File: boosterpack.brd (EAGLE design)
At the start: 100 x 80 mm, 17 parts

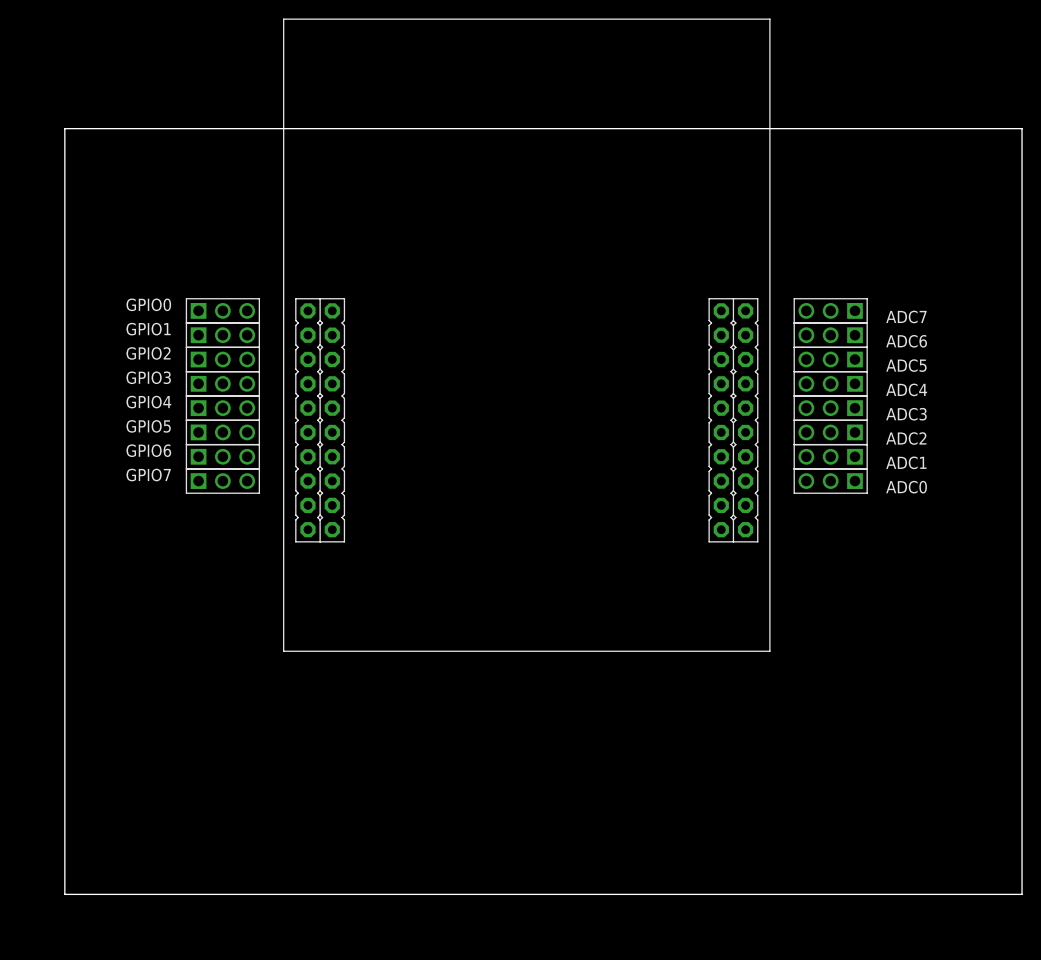
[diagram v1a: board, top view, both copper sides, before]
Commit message: added power regulating circiut
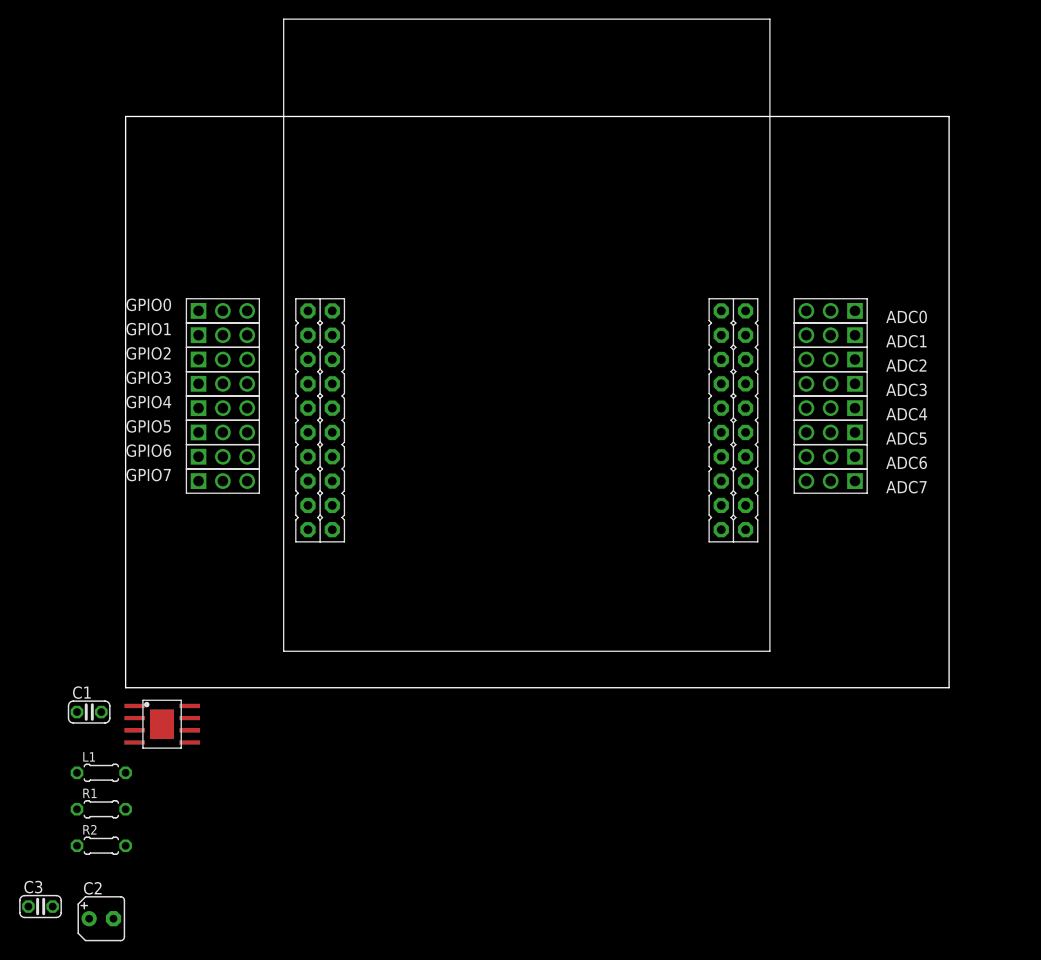
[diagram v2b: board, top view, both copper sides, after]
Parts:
- added C1: 10nF, resistor:C025-024X044
- added C2: 330uF, resistor:B45181A
- added C3: (no value), resistor:C025-024X044
- added L1: 10uH, resistor:0204/5
- added R1: 10k, resistor:0204/5
- added R2: 3.24k, resistor:0204/5
- added U$2: TPS5450, packages(ti):DDS
- moved ADC0 17.8 mm to (82.5, 61.0)
- moved ADC7 17.8 mm to (82.5, 43.2)
- moved ADC1 12.7 mm to (82.5, 58.4)
- moved ADC6 12.7 mm to (82.5, 45.7)
- moved ADC2 7.62 mm to (82.5, 55.9)
- moved ADC5 7.62 mm to (82.5, 48.3)
- moved ADC3 2.54 mm to (82.5, 53.3)
- moved ADC4 2.54 mm to (82.5, 50.8)
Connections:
- removed net GND2: U$1.GND2
- removed net VBUS: U$1.VBUS
- new net +5V: C2.+, L1.2, R1.2, U$1.VBUS
- new net GND: C2.-, C3.2, R2.1, U$1.GND1, U$1.GND2, U$2.6, U$2.GROUNDPAD
- new net N$10: R1.1, R2.2, U$2.4
- new net N$11: C1.1, L1.1, U$2.8
- new net N$9: C1.2, U$2.1
- new net VCC: C3.1, U$2.7
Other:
- board size 100 x 80 mm -> 86 x 59.7 mm
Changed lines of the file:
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@@
 <board>
 <plain>
-<wire x1="0" y1="0" x2="100" y2="0" width="0" layer="20"/>
-<wire x1="100" y1="0" x2="100" y2="80" width="0" layer="20"/>
-<wire x1="100" y1="80" x2="0" y2="80" width="0" layer="20"/>
-<wire x1="0" y1="80" x2="0" y2="0" width="0" layer="20"/>
+<wire x1="6.35" y1="21.59" x2="92.38" y2="21.59" width="0" layer="20"/>
+<wire x1="92.38" y1="21.59" x2="92.38" y2="81.27" width="0" layer="20"/>
+<wire x1="92.38" y1="81.27" x2="6.35" y2="81.27" width="0" layer="20"/>
+<wire x1="6.35" y1="81.27" x2="6.35" y2="21.59" width="0" layer="20"/>
 </plain>
 <attributes>
@@
 <element name="GPIO7" library="RASEagleLib" package="3PINHEADER" value="3PINHEADER" x="13.97" y="43.18"/>
 <element name="GPIO5" library="RASEagleLib" package="3PINHEADER" value="3PINHEADER" x="13.97" y="48.26"/>
-<element name="ADC0" library="RASEagleLib" package="3PINHEADER" value="3PINHEADER" x="82.55" y="43.18" rot="R180"/>
-<element name="ADC2" library="RASEagleLib" package="3PINHEADER" value="3PINHEADER" x="82.55" y="48.26" rot="R180"/>
-<element name="ADC1" library="RASEagleLib" package="3PINHEADER" value="3PINHEADER" x="82.55" y="45.72" rot="R180"/>
-<element name="ADC3" library="RASEagleLib" package="3PINHEADER" value="3PINHEADER" x="82.55" y="50.8" rot="R180"/>
-<element name="ADC7" library="RASEagleLib" package="3PINHEADER" value="3PINHEADER" x="82.55" y="60.96" rot="R180"/>
-<element name="ADC6" library="RASEagleLib" package="3PINHEADER" value="3PINHEADER" x="82.55" y="58.42" rot="R180"/>
-<element name="ADC5" library="RASEagleLib" package="3PINHEADER" value="3PINHEADER" x="82.55" y="55.88" rot="R180"/>
-<element name="ADC4" library="RASEagleLib" package="3PINHEADER" value="3PINHEADER" x="82.55" y="53.34" rot="R180"/>
+<element name="ADC0" library="RASEagleLib" package="3PINHEADER" value="3PINHEADER" x="82.55" y="60.96" rot="R180"/>
+<element name="ADC2" library="RASEagleLib" package="3PINHEADER" value="3PINHEADER" x="82.55" y="55.88" rot="R180"/>
+<element name="ADC1" library="RASEagleLib" package="3PINHEADER" value="3PINHEADER" x="82.55" y="58.42" rot="R180"/>
+<element name="ADC3" library="RASEagleLib" package="3PINHEADER" value="3PINHEADER" x="82.55" y="53.34" rot="R180"/>
+<element name="ADC7" library="RASEagleLib" package="3PINHEADER" value="3PINHEADER" x="82.55" y="43.18" rot="R180"/>
+<element name="ADC6" library="RASEagleLib" package="3PINHEADER" value="3PINHEADER" x="82.55" y="45.72" rot="R180"/>
+<element name="ADC5" library="RASEagleLib" package="3PINHEADER" value="3PINHEADER" x="82.55" y="48.26" rot="R180"/>
+<element name="ADC4" library="RASEagleLib" package="3PINHEADER" value="3PINHEADER" x="82.55" y="50.8" rot="R180"/>
+<element name="U$2" library="packages(ti)" package="DDS" value="TPS5450" x="10.16" y="17.78"/>
+<element name="C1" library="resistor" package="C025-024X044" value="10nF" x="2.54" y="19.05"/>
+<element name="L1" library="resistor" package="0204/5" value="10uH" x="3.81" y="12.7"/>
+<element name="R1" library="resistor" package="0204/5" value="10k" x="3.81" y="8.89"/>
+<element name="R2" library="resistor" package="0204/5" value="3.24k" x="3.81" y="5.08"/>
+<element name="C2" library="resistor" package="B45181A" value="330uF" x="3.81" y="-2.54"/>
+<element name="C3" library="resistor" package="C025-024X044" value="" x="-2.54" y="-1.27"/>
 </elements>
 <signals>
@@
 <contactref element="U$1" pad="3.3V"/>
 </signal>
-<signal name="VBUS">
-<contactref element="U$1" pad="VBUS"/>
-</signal>
 <signal name="RST">
 <contactref element="U$1" pad="RST"/>
-</signal>
-<signal name="GND2">
-<contactref element="U$1" pad="GND2"/>
 </signal>
 <signal name="N$7">
@@
 <contactref element="U$1" pad="PB7"/>
 </signal>
+<signal name="N$9">
+<contactref element="U$2" pad="1"/>
+<contactref element="C1" pad="2"/>
+<wire x1="3.81" y1="19.05" x2="7.285" y2="19.685" width="0" layer="19" extent="1-1"/>
+</signal>
+<signal name="+5V">
+<contactref element="C2" pad="+"/>
+<contactref element="L1" pad="2"/>
+<contactref element="R1" pad="2"/>
+<contactref element="U$1" pad="VBUS"/>
+<wire x1="6.35" y1="12.7" x2="27.94" y2="60.96" width="0" layer="19" extent="1-1"/>
+<wire x1="6.35" y1="8.89" x2="6.35" y2="12.7" width="0" layer="19" extent="1-1"/>
+<wire x1="2.54" y1="-2.54" x2="6.35" y2="8.89" width="0" layer="19" extent="1-1"/>
+</signal>
+<signal name="GND">
+<contactref element="C2" pad="-"/>
+<contactref element="R2" pad="1"/>
+<contactref element="C3" pad="2"/>
+<contactref element="U$2" pad="6"/>
+<contactref element="U$2" pad="GROUNDPAD"/>
+<contactref element="U$1" pad="GND1"/>
+<contactref element="U$1" pad="GND2"/>
+<wire x1="27.94" y1="58.42" x2="71.12" y2="60.96" width="0" layer="19" extent="1-1"/>
+<wire x1="13.035" y1="17.145" x2="27.94" y2="58.42" width="0" layer="19" extent="1-1"/>
+<wire x1="10.16" y1="17.78" x2="13.035" y2="17.145" width="0" layer="19" extent="1-1"/>
+<wire x1="1.27" y1="5.08" x2="10.16" y2="17.78" width="0" layer="19" extent="1-1"/>
+<wire x1="-1.27" y1="-1.27" x2="1.27" y2="5.08" width="0" layer="19" extent="1-1"/>
+<wire x1="5.08" y1="-2.54" x2="-1.27" y2="-1.27" width="0" layer="19" extent="1-1"/>
+</signal>
+<signal name="N$10">
+<contactref element="U$2" pad="4"/>
+<contactref element="R1" pad="1"/>
+<contactref element="R2" pad="2"/>
+<wire x1="1.27" y1="8.89" x2="7.285" y2="15.875" width="0" layer="19" extent="1-1"/>
+<wire x1="6.35" y1="5.08" x2="1.27" y2="8.89" width="0" layer="19" extent="1-1"/>
+</signal>
+<signal name="N$11">
+<contactref element="U$2" pad="8"/>
+<contactref element="L1" pad="1"/>
+<contactref element="C1" pad="1"/>
+<wire x1="1.27" y1="19.05" x2="13.035" y2="19.685" width="0" layer="19" extent="1-1"/>
+<wire x1="1.27" y1="12.7" x2="1.27" y2="19.05" width="0" layer="19" extent="1-1"/>
+</signal>
+<signal name="VCC">
+<contactref element="U$2" pad="7"/>
+<contactref element="C3" pad="1"/>
+<wire x1="-3.81" y1="-1.27" x2="13.035" y2="18.415" width="0" layer="19" extent="1-1"/>
+</signal>
 </signals>

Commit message: new layout for the reg circuit
I feel like explaining my use of the smd inductor
 * it's small ~10mm wide by ~6mm tall
 * it's easy to solder (it's a huge smd part afterall)
 * it's cheip $0.60
 * it makes putting the regulator under the launchpad possible
 * it brings down the surface area by about half compared to other parts
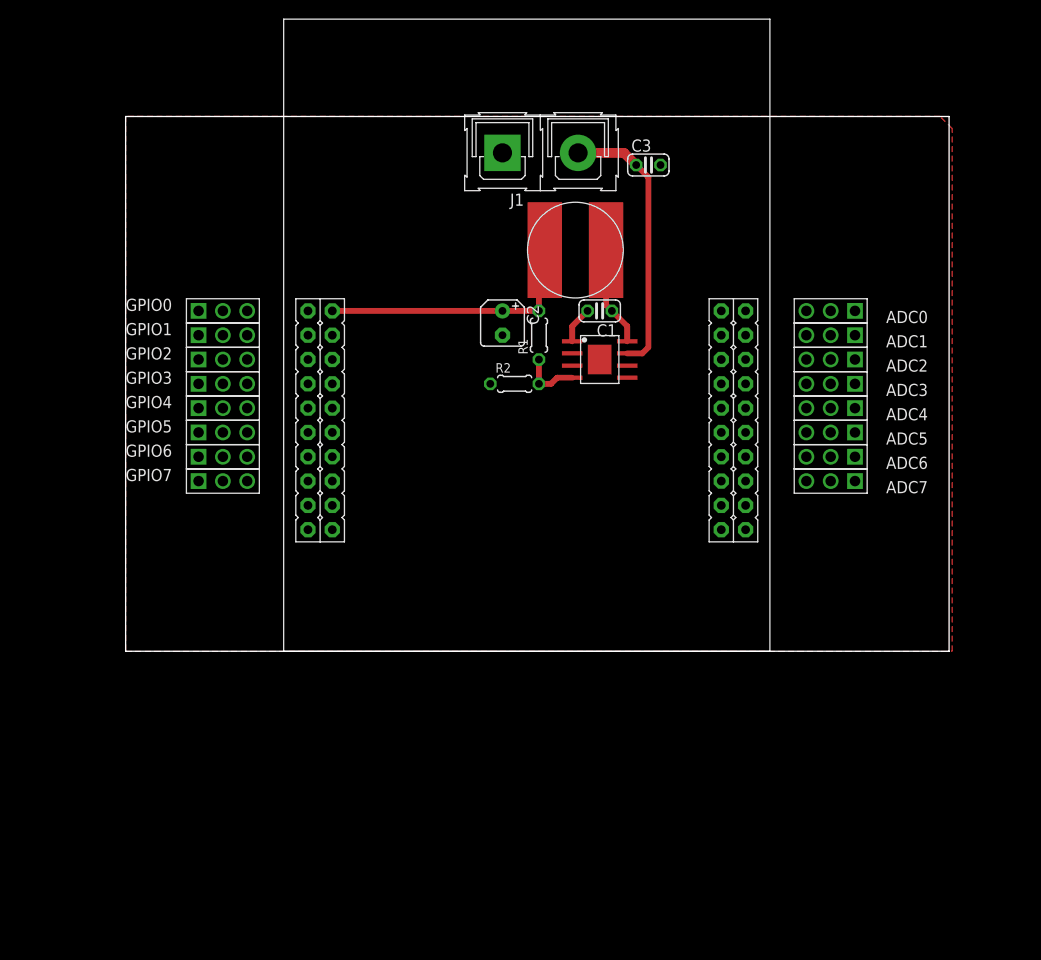
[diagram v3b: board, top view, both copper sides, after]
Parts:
- added J1: POWERPOLE_DOUBLE, RASEagleLib:POWERPOLE_DOUBLE
- L1: device resistor:0204/5 -> RASEagleLib:SDR1006
- moved C3 100.2 mm to (61.0, 76.2)
- moved C2 75.0 mm to (45.7, 59.7), turned to 270 degrees
- moved L1 73.7 mm to (53.3, 67.3), turned to 270 degrees
- moved C1 67.8 mm to (55.9, 61.0), turned to 180 degrees
- moved R1 67.4 mm to (49.5, 58.4), turned to 90 degrees
- moved R2 64.8 mm to (47.0, 53.3)
- moved U$2 59.5 mm to (55.9, 55.9)
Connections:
- net +5V: now also L1.P$2; no longer L1.2
- net GND: now also J1.1
- net N$11: now also L1.P$1; no longer L1.1
- net VCC: now also J1.2
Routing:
- net VCC: track 0.00 -> 28.6 mm
- net +5V: track 0.00 -> 28.2 mm
- net N$11: track 0.00 -> 10.4 mm
- net N$10: track 0.00 -> 6.28 mm
- net N$9: track 0.00 -> 3.84 mm
- added copper zone on layer 1, net GND
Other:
- board size 86 x 59.7 mm -> 86 x 55.9 mm
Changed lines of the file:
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@@
 <board>
 <plain>
-<wire x1="6.35" y1="21.59" x2="92.38" y2="21.59" width="0" layer="20"/>
-<wire x1="92.38" y1="21.59" x2="92.38" y2="81.27" width="0" layer="20"/>
+<wire x1="6.35" y1="25.4" x2="92.38" y2="25.4" width="0" layer="20"/>
+<wire x1="92.38" y1="25.4" x2="92.38" y2="81.27" width="0" layer="20"/>
 <wire x1="92.38" y1="81.27" x2="6.35" y2="81.27" width="0" layer="20"/>
-<wire x1="6.35" y1="81.27" x2="6.35" y2="21.59" width="0" layer="20"/>
+<wire x1="6.35" y1="81.27" x2="6.35" y2="25.4" width="0" layer="20"/>
 </plain>
 <attributes>
@@
 <element name="ADC5" library="RASEagleLib" package="3PINHEADER" value="3PINHEADER" x="82.55" y="48.26" rot="R180"/>
 <element name="ADC4" library="RASEagleLib" package="3PINHEADER" value="3PINHEADER" x="82.55" y="50.8" rot="R180"/>
-<element name="U$2" library="packages(ti)" package="DDS" value="TPS5450" x="10.16" y="17.78"/>
-<element name="C1" library="resistor" package="C025-024X044" value="10nF" x="2.54" y="19.05"/>
-<element name="L1" library="resistor" package="0204/5" value="10uH" x="3.81" y="12.7"/>
-<element name="R1" library="resistor" package="0204/5" value="10k" x="3.81" y="8.89"/>
-<element name="R2" library="resistor" package="0204/5" value="3.24k" x="3.81" y="5.08"/>
-<element name="C2" library="resistor" package="B45181A" value="330uF" x="3.81" y="-2.54"/>
-<element name="C3" library="resistor" package="C025-024X044" value="" x="-2.54" y="-1.27"/>
+<element name="U$2" library="packages(ti)" package="DDS" value="TPS5450" x="55.88" y="55.88"/>
+<element name="C1" library="resistor" package="C025-024X044" value="10nF" x="55.88" y="60.96" rot="R180"/>
+<element name="L1" library="RASEagleLib" package="SDR1006" value="10uH" x="53.34" y="67.31" rot="R270"/>
+<element name="R1" library="resistor" package="0204/5" value="10k" x="49.53" y="58.42" rot="R90"/>
+<element name="R2" library="resistor" package="0204/5" value="3.24k" x="46.99" y="53.34"/>
+<element name="C2" library="resistor" package="B45181A" value="330uF" x="45.72" y="59.69" rot="R270"/>
+<element name="C3" library="resistor" package="C025-024X044" value="" x="60.96" y="76.2"/>
+<element name="J1" library="RASEagleLib" package="POWERPOLE_DOUBLE" value="POWERPOLE_DOUBLE" x="45.72" y="77.47"/>
 </elements>
 <signals>
@@
 <contactref element="U$2" pad="1"/>
 <contactref element="C1" pad="2"/>
-<wire x1="3.81" y1="19.05" x2="7.285" y2="19.685" width="0" layer="19" extent="1-1"/>
+<wire x1="54.61" y1="60.96" x2="53.005" y2="59.355" width="0.6096" layer="1"/>
+<wire x1="53.005" y1="59.355" x2="53.005" y2="57.785" width="0.6096" layer="1"/>
 </signal>
 <signal name="+5V">
 <contactref element="C2" pad="+"/>
-<contactref element="L1" pad="2"/>
+<contactref element="L1" pad="P$2"/>
 <contactref element="R1" pad="2"/>
 <contactref element="U$1" pad="VBUS"/>
-<wire x1="6.35" y1="12.7" x2="27.94" y2="60.96" width="0" layer="19" extent="1-1"/>
-<wire x1="6.35" y1="8.89" x2="6.35" y2="12.7" width="0" layer="19" extent="1-1"/>
-<wire x1="2.54" y1="-2.54" x2="6.35" y2="8.89" width="0" layer="19" extent="1-1"/>
+<wire x1="27.94" y1="60.96" x2="45.72" y2="60.96" width="0.6096" layer="1"/>
+<wire x1="49.53" y1="60.96" x2="45.72" y2="60.96" width="0.6096" layer="1"/>
+<wire x1="49.53" y1="60.96" x2="49.53" y2="64.77" width="0.6096" layer="1"/>
+<wire x1="49.53" y1="64.77" x2="50.14" y2="65.38" width="0.6096" layer="1"/>
+<wire x1="50.14" y1="65.38" x2="50.14" y2="67.31" width="0.6096" layer="1"/>
 </signal>
 <signal name="GND">
@@
 <contactref element="U$1" pad="GND1"/>
 <contactref element="U$1" pad="GND2"/>
-<wire x1="27.94" y1="58.42" x2="71.12" y2="60.96" width="0" layer="19" extent="1-1"/>
-<wire x1="13.035" y1="17.145" x2="27.94" y2="58.42" width="0" layer="19" extent="1-1"/>
-<wire x1="10.16" y1="17.78" x2="13.035" y2="17.145" width="0" layer="19" extent="1-1"/>
-<wire x1="1.27" y1="5.08" x2="10.16" y2="17.78" width="0" layer="19" extent="1-1"/>
-<wire x1="-1.27" y1="-1.27" x2="1.27" y2="5.08" width="0" layer="19" extent="1-1"/>
-<wire x1="5.08" y1="-2.54" x2="-1.27" y2="-1.27" width="0" layer="19" extent="1-1"/>
+<polygon width="0.4064" layer="1" isolate="0.6096">
+<vertex x="6.35" y="81.28"/>
+<vertex x="6.35" y="25.4"/>
+<vertex x="92.71" y="25.4"/>
+<vertex x="92.71" y="80.01"/>
+<vertex x="91.44" y="81.28"/>
+</polygon>
+<contactref element="J1" pad="1"/>
 </signal>
 <signal name="N$10">
@@
 <contactref element="R1" pad="1"/>
 <contactref element="R2" pad="2"/>
-<wire x1="1.27" y1="8.89" x2="7.285" y2="15.875" width="0" layer="19" extent="1-1"/>
-<wire x1="6.35" y1="5.08" x2="1.27" y2="8.89" width="0" layer="19" extent="1-1"/>
+<wire x1="51.435" y1="53.975" x2="53.005" y2="53.975" width="0.6096" layer="1"/>
+<wire x1="49.53" y1="55.88" x2="49.53" y2="53.34" width="0.6096" layer="1"/>
+<wire x1="51.435" y1="53.975" x2="50.8" y2="53.34" width="0.6096" layer="1"/>
+<wire x1="50.8" y1="53.34" x2="49.53" y2="53.34" width="0.6096" layer="1"/>
 </signal>
 <signal name="N$11">
 <contactref element="U$2" pad="8"/>
-<contactref element="L1" pad="1"/>
+<contactref element="L1" pad="P$1"/>
 <contactref element="C1" pad="1"/>
-<wire x1="1.27" y1="19.05" x2="13.035" y2="19.685" width="0" layer="19" extent="1-1"/>
-<wire x1="1.27" y1="12.7" x2="1.27" y2="19.05" width="0" layer="19" extent="1-1"/>
+<wire x1="57.15" y1="60.96" x2="58.755" y2="59.355" width="0.6096" layer="1"/>
+<wire x1="58.755" y1="59.355" x2="58.755" y2="57.785" width="0.6096" layer="1"/>
+<wire x1="57.15" y1="60.96" x2="56.54" y2="61.57" width="0.6096" layer="1"/>
+<wire x1="56.54" y1="61.57" x2="56.54" y2="67.31" width="0.6096" layer="1"/>
 </signal>
 <signal name="VCC">
 <contactref element="U$2" pad="7"/>
 <contactref element="C3" pad="1"/>
-<wire x1="-3.81" y1="-1.27" x2="13.035" y2="18.415" width="0" layer="19" extent="1-1"/>
+<contactref element="J1" pad="2"/>
+<wire x1="53.62" y1="77.47" x2="58.42" y2="77.47" width="1.016" layer="1"/>
+<wire x1="58.42" y1="77.47" x2="59.69" y2="76.2" width="1.016" layer="1"/>
+<wire x1="59.69" y1="76.2" x2="60.96" y2="74.93" width="0.6096" layer="1"/>
+<wire x1="60.96" y1="74.93" x2="60.96" y2="57.15" width="0.6096" layer="1"/>
+<wire x1="60.96" y1="57.15" x2="60.325" y2="56.515" width="0.6096" layer="1"/>
+<wire x1="60.325" y1="56.515" x2="58.755" y2="56.515" width="0.6096" layer="1"/>
 </signal>
 </signals>

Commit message: lots of routing; moustly just routing
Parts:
- added SJ1, SJ2: (no value), jumper:SJ_2
- moved C1 1.80 mm to (54.6, 59.7)
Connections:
- removed net 3.3V: U$1.3.3V
- new net ADC5: ADC5.3, U$1.PE1
- new net N$13: ADC4.3, U$1.PE0
- new net N$16: SJ1.3, SJ2.3, U$1.3.3V
- new net N$4: ADC6.3, U$1.PE2
- new net N$5: ADC7.3, U$1.PE3
- new net RIGHTSIDEPOWER: ADC0.2, ADC1.2, ADC2.2, ADC3.2, ADC4.2, ADC5.2, ADC6.2, ADC7.2, SJ1.2
- net +5V: now also SJ1.1, SJ2.1
- net ADC1: now also ADC1.3
- net ADC2: now also ADC2.3
- net ADC3: now also ADC3.3
- net GND: now also ADC0.1, ADC1.1, ADC2.1, ADC3.1, ADC4.1, ADC5.1, ADC6.1, ADC7.1, GPIO0.1, GPIO1.1, GPIO2.1, GPIO3.1, GPIO4.1, GPIO5.1, GPIO6.1, GPIO7.1
- net GPIO0: now also GPIO0.3
- net GPIO1: now also GPIO1.3
- net GPIO2: now also GPIO2.3
- net GPIO3: now also GPIO3.3
- net N$1: now also ADC0.3
- net N$2: now also GPIO4.3
- net N$3: now also GPIO5.3
- net N$6: now also GPIO6.3
- net N$7: now also GPIO0.2, GPIO1.2, GPIO2.2, GPIO3.2, GPIO4.2, GPIO5.2, GPIO6.2, GPIO7.2, SJ2.2; no longer GPIO0.1
- net N$8: now also GPIO7.3
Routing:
- net GPIO2: track 0.00 -> 85.0 mm
- net ADC3: track 0.00 -> 73.7 mm
- net ADC2: track 0.00 -> 72.2 mm
- net N$8: track 0.00 -> 71.9 mm
- net ADC1: track 0.00 -> 71.5 mm
- net N$6: track 0.00 -> 70.5 mm
- net N$1: track 0.00 -> 70.0 mm
- net GPIO3: track 0.00 -> 69.5 mm
- net ADC5: track 0.00 -> 65.5 mm, vias 0 -> 1
- net N$16: track 0.00 -> 63.6 mm, vias 0 -> 2
- net N$4: track 0.00 -> 63.2 mm, vias 0 -> 1
- net N$5: track 0.00 -> 60.0 mm, vias 0 -> 1
- net +5V: track 28.2 -> 72.2 mm, vias 0 -> 2
- net N$7: track 0.00 -> 24.0 mm
- net RIGHTSIDEPOWER: track 0.00 -> 23.6 mm
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- added copper zone on layer 16, net GND
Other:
- board size 86 x 55.9 mm -> 76.5 x 55.9 mm
- board text added: "0"
- board text added: "1"
- board text added: "2"
- board text added: "3"
- board text added: "3V3"
- board text added: "4"
- board text added: "5"
- board text added: "5V"
- board text added: "6"
- board text added: "7"
- board text added: "Ground"
- board text added: "Port B"
- board text added: "Port D"
- board text added: "Port E"
- board text added: "Power"
- board text added: "Signal"
